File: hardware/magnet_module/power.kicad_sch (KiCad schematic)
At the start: 18 parts, among them J20 Barrel_Jack, U11 MIC5219-3.3YM5, U12 TPS565208

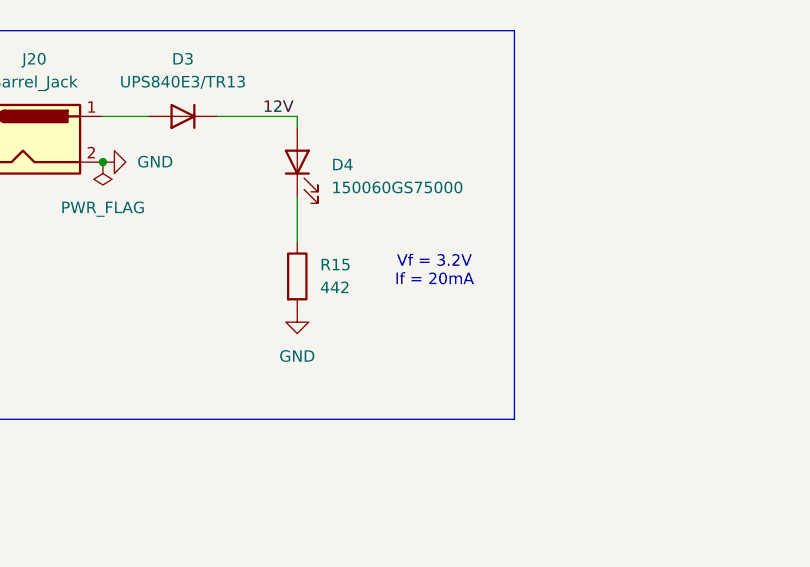
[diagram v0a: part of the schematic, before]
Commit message: change power LED brightness, move level shifter to servo page
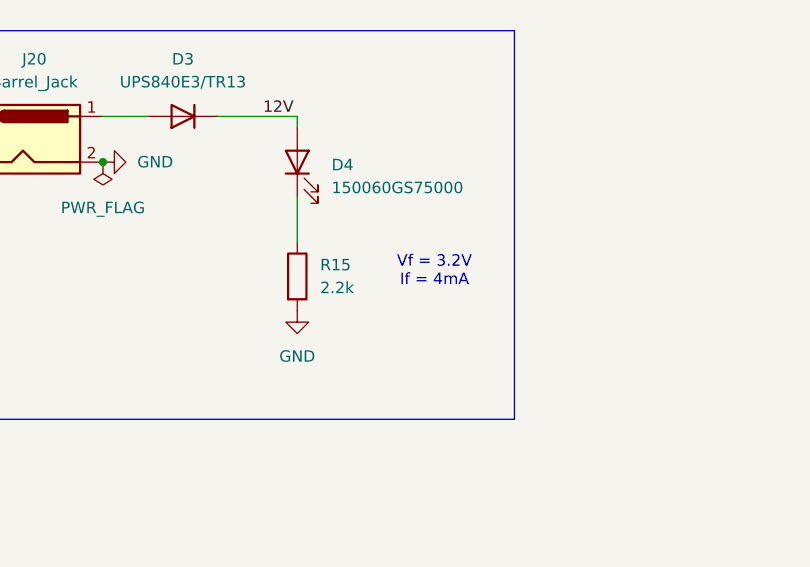
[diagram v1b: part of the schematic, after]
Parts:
- R15: value 442 -> 2.2k
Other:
- note added: "Vf = 3.2V If = 4mA"
- note removed: "Vf = 3.2V If = 20mA"
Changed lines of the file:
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@@
 		)
 	)
-	(text "Vf = 3.2V\nIf = 20mA"
+	(text "Vf = 3.2V\nIf = 4mA"
 		(exclude_from_sim no)
 		(at 76.2 45.212 0)
@@
 			)
 		)
-		(property "Value" "442"
+		(property "Value" "2.2k"
 			(at 63.5 46.9899 0)
 			(effects

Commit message: add titles & esd protection for IO
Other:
- company: (none) -> Christie Lab, CU-Anschultz
- title: (none) -> Autotrainer Magnet Module - Power
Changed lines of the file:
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@@
 	(generator_version "8.0")
 	(paper "A4")
+	(title_block
+		(title "Autotrainer Magnet Module - Power")
+		(date "2024-07-09")
+		(rev "v1.0")
+		(company "Christie Lab, CU-Anschultz")
+		(comment 1 "Prepared by LeafLabs, LLC")
+	)
 	(junction
 		(at 193.04 85.09)

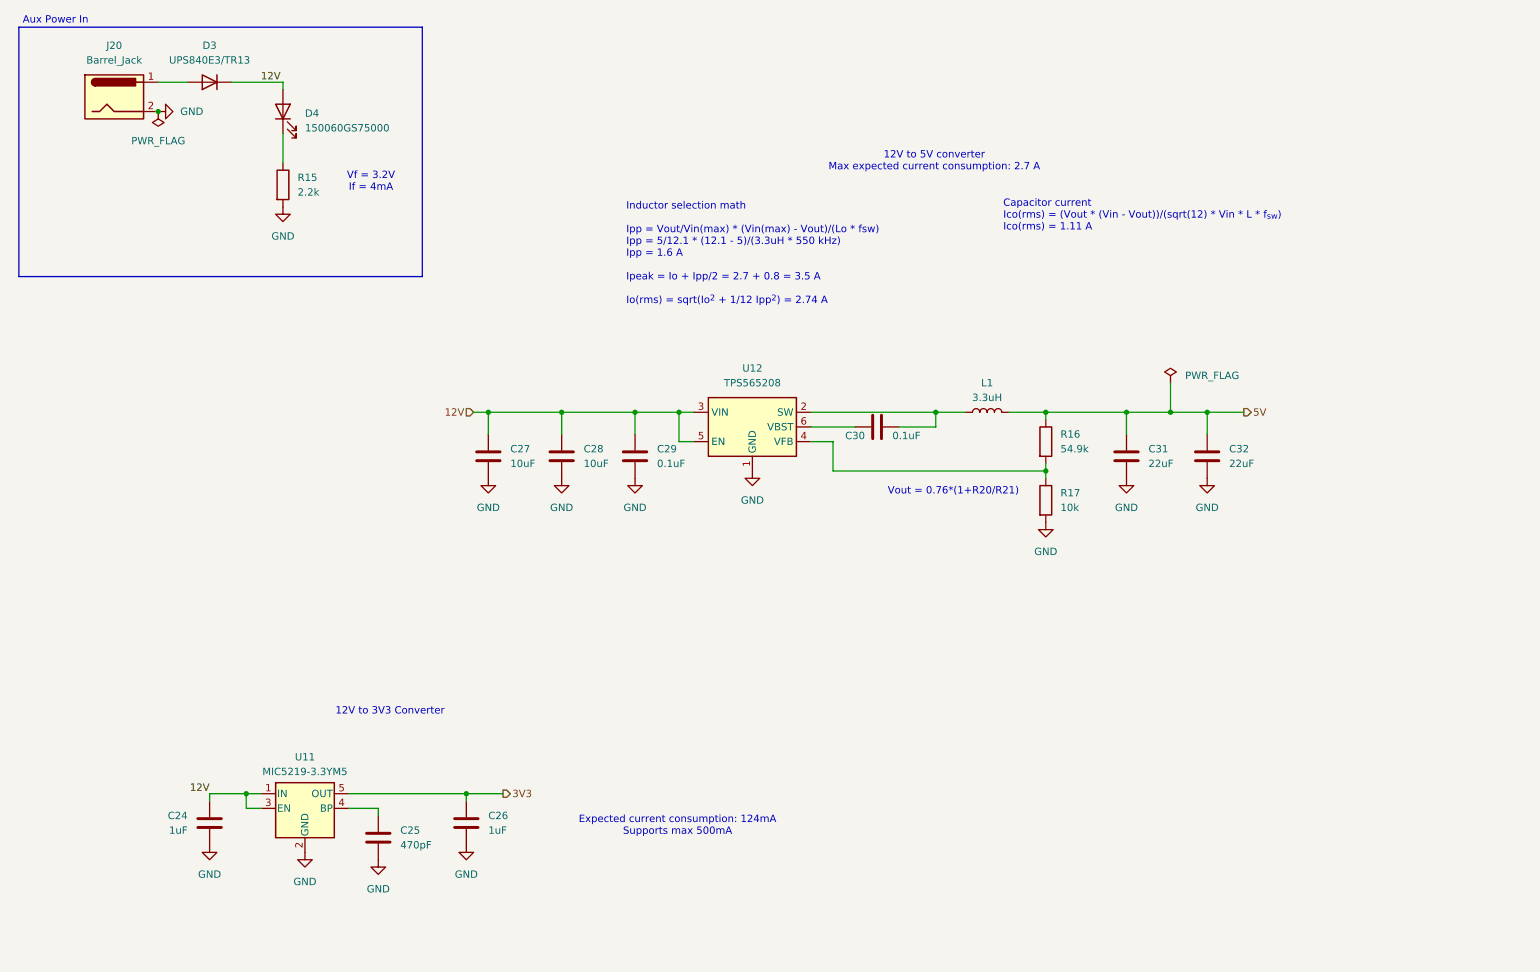
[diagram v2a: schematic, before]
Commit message: add all PNs, relevant datasheets, and test points
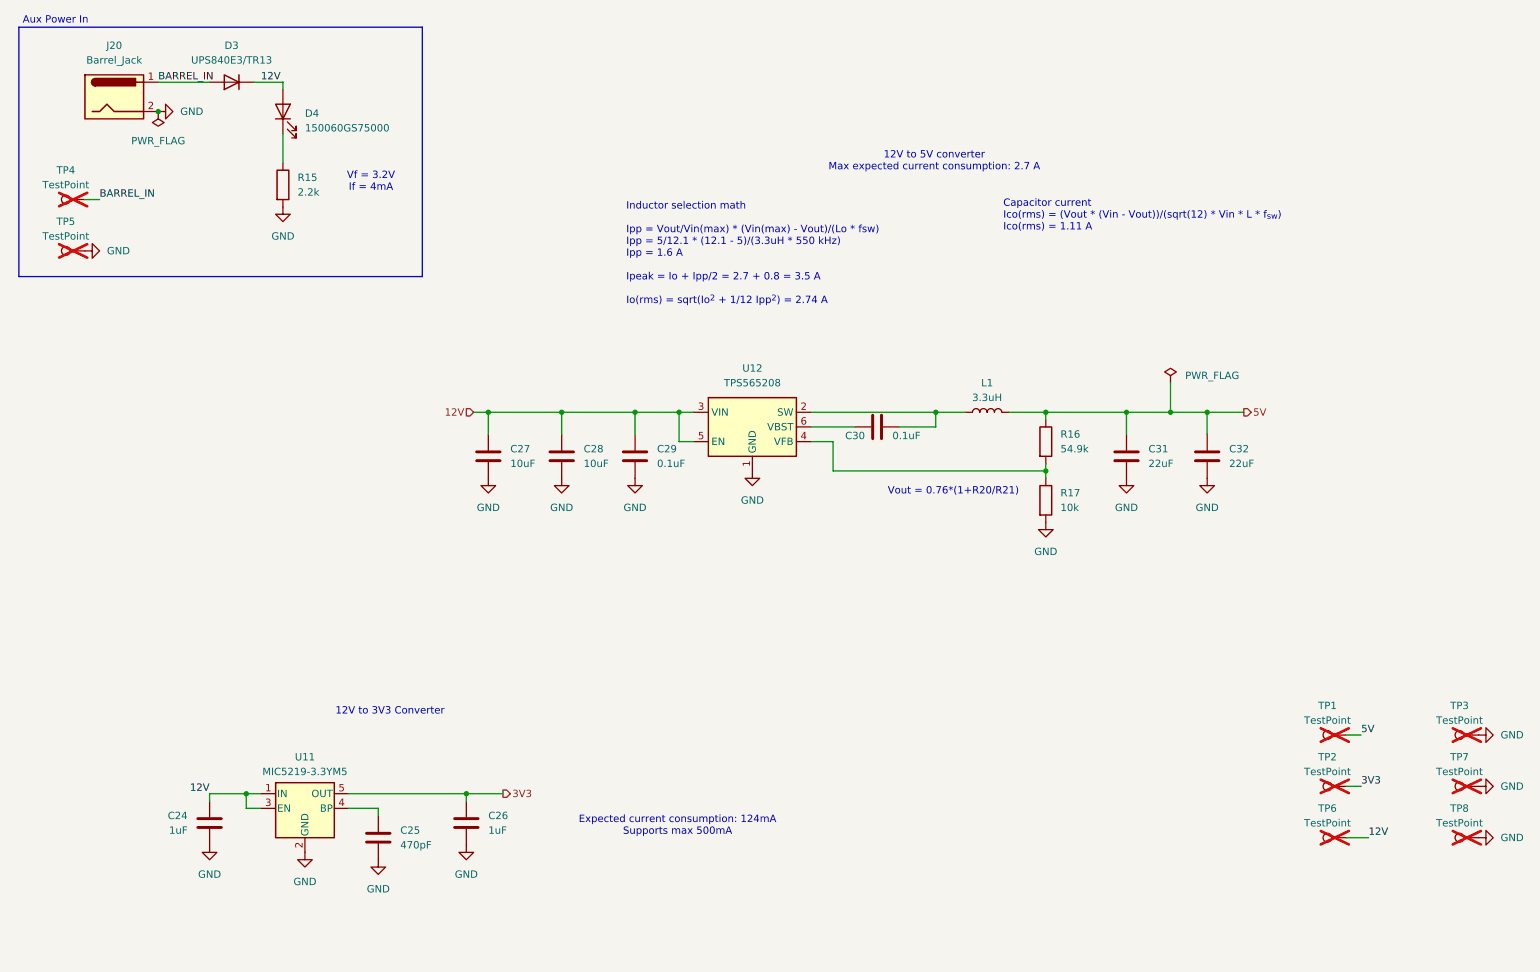
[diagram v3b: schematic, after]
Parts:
- added TP1, TP2, TP3, TP4, TP5, TP6, TP7, TP8: TestPoint, symbol Connector:TestPoint
- C24, C26, C29, C30: footprint (none) -> Capacitor_SMD:C_0603_1608Metric; MPN (none) -> CC0603KRX7R7BB104
- C25: footprint (none) -> Capacitor_SMD:C_0603_1608Metric; MPN (none) -> CL10C471JB8NNNC
- C27, C28: footprint (none) -> Capacitor_SMD:C_0603_1608Metric; MPN (none) -> GRM188R61E106KA73D
- C31, C32: footprint (none) -> Capacitor_SMD:C_0603_1608Metric; MPN (none) -> CL10A226MP8NUNE
- D3: footprint (none) -> Diode_SMD:D_Powermite3; MPN (none) -> UPS840E3/TR13
- D4: footprint (none) -> Diode_SMD:D_0603_1608Metric; MPN (none) -> 150060GS75000
- J20: MPN (none) -> DCJ200-10-A-K1-K
- R15: MPN (none) -> RC0603FR-072K2L
- R16: MPN (none) -> RC0603FR-0754K9L
- R17: MPN (none) -> RC0603FR-0710KL
- U11: MPN (none) -> MIC5219-3.3YM5
- U12: MPN (none) -> TPS565208DDCR
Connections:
- net 12V: now also TP6.1
- net 3V3: now also TP2.1
- net 5V: now also TP1.1
- net GND: now also TP3.1, TP5.1, TP7.1, TP8.1
- net BARREL_IN: now reaches D3.2 (A), J20.1
- net BARREL_IN: now also TP4.1
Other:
- moved on the sheet: D3

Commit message: make changes as requested by Ryan
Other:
- company: Christie Lab, CU-Anschultz -> Christie Lab, CU-Anschutz
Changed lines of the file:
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@@
 		(date "2024-07-09")
 		(rev "v1.0")
-		(company "Christie Lab, CU-Anschultz")
+		(company "Christie Lab, CU-Anschutz")
 		(comment 1 "Prepared by LeafLabs, LLC")
 	)

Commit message: make changes requested by dan, run ERC
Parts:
- TP1, TP2, TP3, TP4, TP5, TP6, TP7, TP8: now fitted; now left out of the parts list
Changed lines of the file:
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@@
 		(unit 1)
 		(exclude_from_sim no)
-		(in_bom yes)
-		(on_board yes)
-		(dnp yes)
+		(in_bom no)
+		(on_board yes)
+		(dnp no)
 		(fields_autoplaced yes)
 		(property "Reference" "TP7"
@@
 		(unit 1)
 		(exclude_from_sim no)
-		(in_bom yes)
-		(on_board yes)
-		(dnp yes)
-		(fields_autoplaced yes)
+		(in_bom no)
+		(on_board yes)
+		(dnp no)
 		(property "Reference" "TP1"
 			(at 241.808 135.89 90)
@@
 		(unit 1)
 		(exclude_from_sim no)
-		(in_bom yes)
-		(on_board yes)
-		(dnp yes)
+		(in_bom no)
+		(on_board yes)
+		(dnp no)
 		(fields_autoplaced yes)
 		(property "Reference" "TP4"
@@
 		(unit 1)
 		(exclude_from_sim no)
-		(in_bom yes)
-		(on_board yes)
-		(dnp yes)
+		(in_bom no)
+		(on_board yes)
+		(dnp no)
 		(fields_autoplaced yes)
 		(property "Reference" "TP2"
@@
 		(unit 1)
 		(exclude_from_sim no)
-		(in_bom yes)
-		(on_board yes)
-		(dnp yes)
+		(in_bom no)
+		(on_board yes)
+		(dnp no)
 		(fields_autoplaced yes)
 		(property "Reference" "TP6"
@@
 		(unit 1)
 		(exclude_from_sim no)
-		(in_bom yes)
-		(on_board yes)
-		(dnp yes)
+		(in_bom no)
+		(on_board yes)
+		(dnp no)
 		(fields_autoplaced yes)
 		(property "Reference" "TP8"
@@
 		(unit 1)
 		(exclude_from_sim no)
-		(in_bom yes)
-		(on_board yes)
-		(dnp yes)
+		(in_bom no)
+		(on_board yes)
+		(dnp no)
 		(fields_autoplaced yes)
 		(property "Reference" "TP3"
@@
 		(unit 1)
 		(exclude_from_sim no)
-		(in_bom yes)
-		(on_board yes)
-		(dnp yes)
+		(in_bom no)
+		(on_board yes)
+		(dnp no)
 		(fields_autoplaced yes)
 		(property "Reference" "TP5"

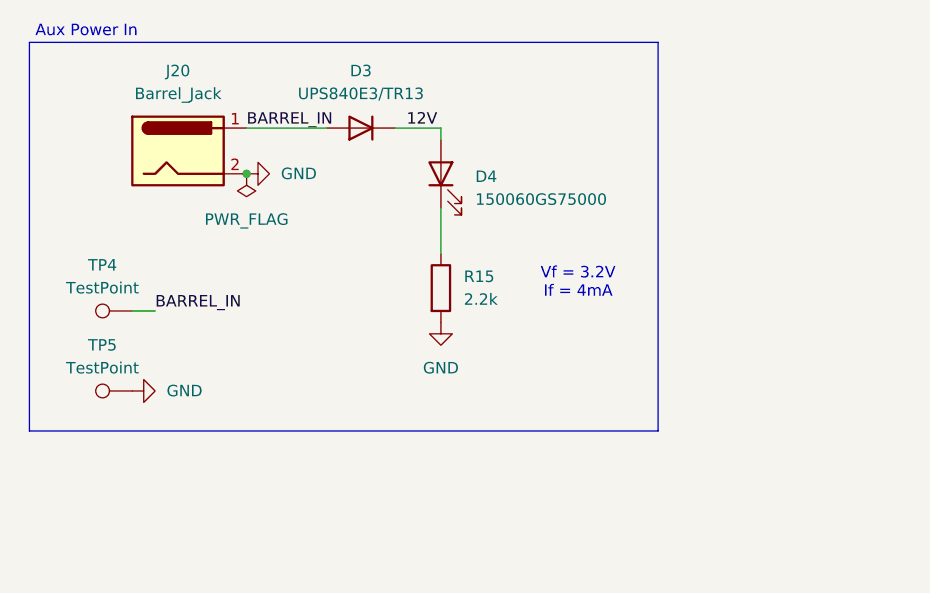
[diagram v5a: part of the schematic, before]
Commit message: add footprints & 3d models for magnet module connector placmeent
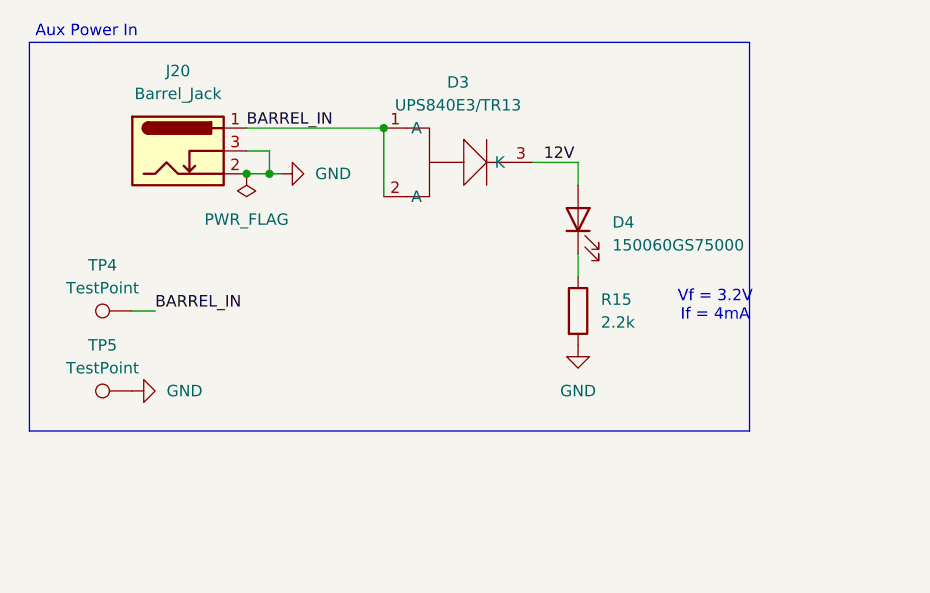
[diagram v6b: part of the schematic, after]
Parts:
- D3: symbol Device:D -> Leaf_Diode:Diode_123
- J20: footprint (none) -> Connector_BarrelJack:BarrelJack_GCT_DCJ200-10-A_Horizontal; symbol Connector:Barrel_Jack -> Connector:Barrel_Jack_Switch
- L1: footprint (none) -> Inductor_SMD:L_TDK_VLS6045EX_VLS6045AF; MPN NRS5030T3R3MMGJ -> VLS6045EX-3R3N
- R15, R16, R17: footprint (none) -> Resistor_SMD:R_0603_1608Metric
- TP1, TP2, TP3, TP4, TP5, TP6, TP7, TP8: footprint (none) -> TestPoint:TestPoint_Pad_1.0x1.0mm
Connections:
- net 12V: now also D3.3 (K); no longer D3.1 (K)
- net BARREL_IN: now also D3.1 (A)
- net GND: now also J20.3
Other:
- moved on the sheet: D4, R15

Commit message: Releases layout for pellet, magnet, and Jetson breakout boards.
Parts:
- removed C24, C26: 1uF, Capacitor_SMD:C_0603_1608Metric, symbol Device:C
- removed C25: 470pF, Capacitor_SMD:C_0603_1608Metric, symbol Device:C
- removed U11: MIC5219-3.3YM5, Package_TO_SOT_SMD:SOT-23-5, symbol Regulator_Linear:MIC5219-3.3YM5
- added C20: 10uF, Capacitor_SMD:C_0603_1608Metric, symbol Device:C
- added C21: 0.1uF, Capacitor_SMD:C_0603_1608Metric, symbol Device:C
- added C23, C33: 22uF, Capacitor_SMD:C_0603_1608Metric, symbol Device:C
- added L2: 3.3uH, Leaf_Inductor:L_Taiyo_Yuden_MAMK, symbol Device:L
- added R12: 33.2k, Resistor_SMD:R_0603_1608Metric, symbol Device:R
- added R13: 10k, Resistor_SMD:R_0603_1608Metric, symbol Device:R
- added U9: TPS561201, Package_TO_SOT_SMD:SOT-23-6, symbol Leaf_Regulator:TPS56120x
- C27, C28: LCSC (none) -> C96446; MPN GRM188R61E106KA73D -> CL10A106MA8NRNC
- C29, C30: LCSC (none) -> C14663; MPN CC0603KRX7R7BB104 -> CC0603KRX7R9BB104
- C31, C32: LCSC (none) -> C59461; MPN CL10A226MP8NUNE -> CL10A226MQ8NRNC
- D3: footprint Diode_SMD:D_Powermite3 -> Leaf_Diode:POWERMITE3_MCH; LCSC (none) -> C3758317
- D4: LCSC (none) -> C5252984
- J20: LCSC (none) -> C5280493
- L1: LCSC (none) -> C307879
- R15: LCSC (none) -> C4190; MPN RC0603FR-072K2L -> 0603WAF2201T5E
- R16: LCSC (none) -> C23077; MPN RC0603FR-0754K9L -> 0603WAF5492T5E
- R17: LCSC (none) -> C25804; MPN RC0603FR-0710KL -> 0603WAF1002T5E
- U12: LCSC (none) -> C2650336
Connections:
- net 12V: now also C20.1, U9.3 (VIN), U9.5 (EN)
- net 3V3: now also C23.1, C33.1, L2.2, R12.1
- net GND: now also C20.2, C23.2, C33.2, R13.2, U9.1 (GND)
- new net: C21.1, U9.6 (VBST)
- new net: C21.2, L2.1, U9.2 (SW)
- new net: R12.2, R13.1, U9.4 (VFB)
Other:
- note added: "Expected current consumption: 126mA Supports max 500mA"
- note added: "Ipp = 3.3/12.1 * (12.1 - 3.3)/(3.3uH * 580kHz) = 1.25 A Ipeak = 0.5 + 1.25/2 = 1.125 A Ilo(rms) = sqrt(0.5^{2}+1/12 Ipp^{2})= 0.62 A"
- note added: "RLC component values suggested in datasheet"
- note added: "Vout = 0.76*(1+R20/R21) Vout = 4.93V"
- note removed: "Expected current consumption: 124mA Supports max 500mA"
- note removed: "Vout = 0.76*(1+R20/R21)"
